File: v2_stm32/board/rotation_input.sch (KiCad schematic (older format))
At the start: 0 parts

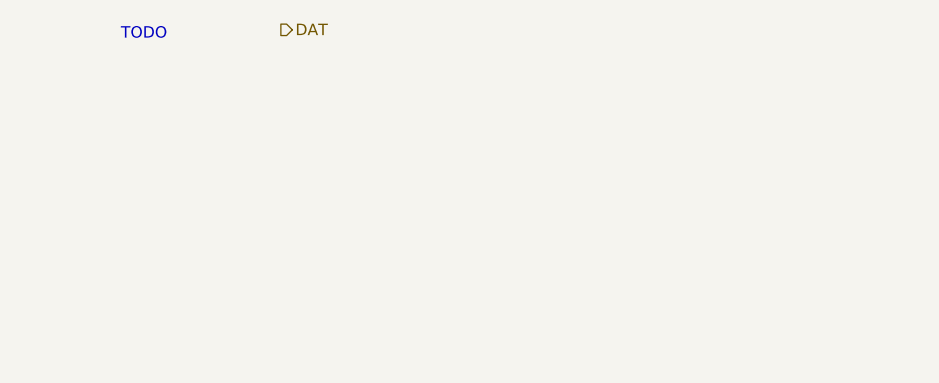
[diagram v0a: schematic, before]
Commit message: Schematic finished (V0.1), Added footprints
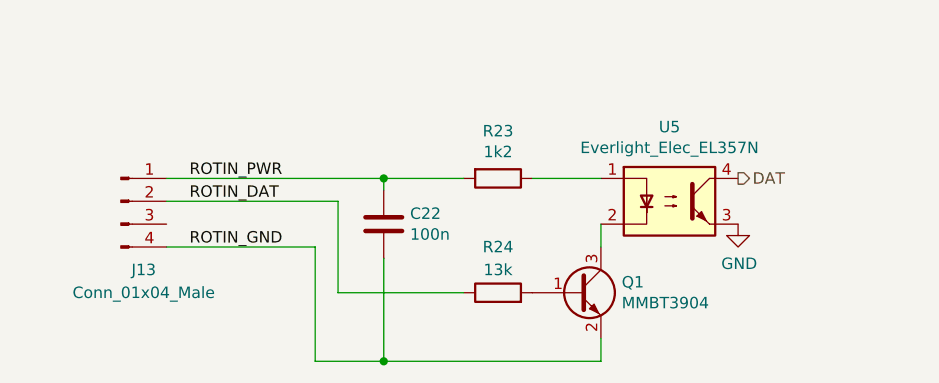
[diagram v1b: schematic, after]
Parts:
- added C22: 100n, Capacitor_SMD:C_0603_1608Metric, symbol Device:C
- added J13: Conn_01x04_Male, Connector_PinHeader_2.54mm:PinHeader_1x04_P2.54mm_Horizontal, symbol Connector:Conn_01x04_Male
- added Q1: MMBT3904, Package_TO_SOT_SMD:SOT-23, symbol Transistor_BJT:MMBT3904
- added R23: 1k2, Resistor_SMD:R_0805_2012Metric, symbol Device:R
- added R24: 13k, Resistor_SMD:R_0603_1608Metric, symbol Device:R
- added U5: Everlight_Elec_EL357N, Lathecontrol_STM32:SOP-4_4.1x4.4x2.54P, symbol Lathecontrol_STM32:Everlight_Elec_EL357N
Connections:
- net DAT: now also U5.4
- new net: Q1.1 (B), R24.2
- new net: Q1.3 (C), U5.2
- new net: R23.1, U5.1
- new net GND: U5.3
- new net ROTIN_DAT: J13.2 (Pin_2), R24.1
- new net ROTIN_GND: C22.2, J13.4 (Pin_4), Q1.2 (E)
- new net ROTIN_PWR: C22.1, J13.1 (Pin_1), R23.2
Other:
- note removed: "TODO"
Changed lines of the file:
@@
 Comment4 ""
 $EndDescr
-Text HLabel 2500 1150 2    50   Output ~ 0
+Text HLabel 4500 1800 2    50   Output ~ 0
 DAT
-Text Notes 1800 1200 0    50   ~ 0
-TODO
+$Comp
+L Lathecontrol_STM32:Everlight_Elec_EL357N U5
+U 1 1 60817786
+P 4200 1900
+F 0 "U5" H 4200 2225 50  0000 C CNN
+F 1 "Everlight_Elec_EL357N" H 4200 2134 50  0000 C CNN
+F 2 "Lathecontrol_STM32:SOP-4_4.1x4.4x2.54P" H 4000 1700 50  0001 L CIN
+F 3 "https://datasheet.lcsc.com/szlcsc/Everlight-Elec-EL357N-B-TA-G_C6649.pdf" H 4200 1900 50  0001 L CNN
+F 4 "C6649" H 4200 1900 50  0001 C CNN "LCSC"
+	1    4200 1900
+	1    0    0    -1
+$EndComp
+$Comp
+L power:GND #PWR089
+U 1 1 6034BC3E
+P 4500 2000
+F 0 "#PWR089" H 4500 1750 50  0001 C CNN
+F 1 "GND" H 4505 1827 50  0000 C CNN
+F 2 "" H 4500 2000 50  0001 C CNN
+F 3 "" H 4500 2000 50  0001 C CNN
+	1    4500 2000
+	1    0    0    -1
+$EndComp
+$Comp
+L Transistor_BJT:MMBT3904 Q1
+U 1 1 60328B9E
+P 3800 2300
+F 0 "Q1" H 3991 2346 50  0000 L CNN
+F 1 "MMBT3904" H 3991 2255 50  0000 L CNN
+F 2 "Package_TO_SOT_SMD:SOT-23" H 4000 2225 50  0001 L CIN
+F 3 "https://www.onsemi.com/pub/Collateral/2N3903-D.PDF" H 3800 2300 50  0001 L CNN
+	1    3800 2300
+	1    0    0    -1
+$EndComp
+Wire Wire Line
+	3900 2000 3900 2100
+$Comp
+L Device:R R23
+U 1 1 6032C873
+P 3450 1800
+F 0 "R23" V 3243 1800 50  0000 C CNN
+F 1 "1k2" V 3334 1800 50  0000 C CNN
+F 2 "Resistor_SMD:R_0805_2012Metric" V 3380 1800 50  0001 C CNN
+F 3 "https://datasheet.lcsc.com/szlcsc/Uniroyal-Elec-0805W8F1201T5E_C17379.pdf" H 3450 1800 50  0001 C CNN
+F 4 "C17379" V 3450 1800 50  0001 C CNN "LCSC"
+	1    3450 1800
+	0    1    1    0
+$EndComp
+Wire Wire Line
+	3600 1800 3900 1800
+$Comp
+L Connector:Conn_01x04_Male J13
+U 1 1 6032E605
+P 1800 1900
+F 0 "J13" H 1900 1600 50  0000 C CNN
+F 1 "Conn_01x04_Male" H 1900 1500 50  0000 C CNN
+F 2 "Connector_PinHeader_2.54mm:PinHeader_1x04_P2.54mm_Horizontal" H 1800 1900 50  0001 C CNN
+F 3 "~" H 1800 1900 50  0001 C CNN
+	1    1800 1900
+	1    0    0    -1
+$EndComp
+Wire Wire Line
+	3900 2500 3900 2600
+Text Label 2100 1800 0    50   ~ 0
+ROTIN_PWR
+Wire Wire Line
+	2750 1900 2750 2300
+Wire Wire Line
+	2000 1900 2750 1900
+Wire Wire Line
+	2000 2100 2650 2100
+Wire Wire Line
+	2650 2100 2650 2600
+Text Label 2100 1900 0    50   ~ 0
+ROTIN_DAT
+Text Label 2100 2100 0    50   ~ 0
+ROTIN_GND
+$Comp
+L Device:C C?
+U 1 1 60340E1E
+P 2950 2000
+AR Path="/6025D9E2/60340E1E" Ref="C?"  Part="1"
+AR Path="/6025D9E2/6025E7C0/60340E1E" Ref="C?"  Part="1"
+AR Path="/6025D9E2/60265A76/60340E1E" Ref="C?"  Part="1"
+AR Path="/6025D9E2/60265B58/60340E1E" Ref="C?"  Part="1"
+AR Path="/6025D9E2/60265BB4/60340E1E" Ref="C?"  Part="1"
+AR Path="/6025D9E2/60265C25/60340E1E" Ref="C?"  Part="1"
+AR Path="/60265C89/60340E1E" Ref="C?"  Part="1"
+AR Path="/60265F6D/60340E1E" Ref="C?"  Part="1"
+AR Path="/60265FC9/60340E1E" Ref="C?"  Part="1"
+AR Path="/6026601C/60340E1E" Ref="C?"  Part="1"
+AR Path="/60340E1E" Ref="C?"  Part="1"
+AR Path="/604E4D29/60340E1E" Ref="C22"  Part="1"
+F 0 "C22" H 3065 2046 50  0000 L CNN
+F 1 "100n" H 3065 1955 50  0000 L CNN
+F 2 "Capacitor_SMD:C_0603_1608Metric" H 2988 1850 50  0001 C CNN
+F 3 "https://datasheet.lcsc.com/szlcsc/YAGEO-CC0603KRX7R9BB104_C14663.pdf" H 2950 2000 50  0001 C CNN
+F 4 "C14663" H 2950 2000 50  0001 C CNN "LCSC"
+	1    2950 2000
+	1    0    0    -1
+$EndComp
+Wire Wire Line
+	2000 1800 2950 1800
+Wire Wire Line
+	2950 1800 2950 1850
+Connection ~ 2950 1800
+Wire Wire Line
+	2950 1800 3300 1800
+Wire Wire Line
+	2950 2150 2950 2600
+Wire Wire Line
+	2950 2600 3900 2600
+Wire Wire Line
+	2650 2600 2950 2600
+Connection ~ 2950 2600
+Wire Wire Line
+	2750 2300 3300 2300
+$Comp
+L Device:R R?
+U 1 1 6037DC52
+P 3450 2300
+AR Path="/6025D9E2/6037DC52" Ref="R?"  Part="1"
+AR Path="/6025D9E2/6025E7C0/6037DC52" Ref="R?"  Part="1"
+AR Path="/6025D9E2/60265A76/6037DC52" Ref="R?"  Part="1"
+AR Path="/6025D9E2/60265B58/6037DC52" Ref="R?"  Part="1"
+AR Path="/6025D9E2/60265BB4/6037DC52" Ref="R?"  Part="1"
+AR Path="/6025D9E2/60265C25/6037DC52" Ref="R?"  Part="1"
+AR Path="/60265C89/6037DC52" Ref="R?"  Part="1"
+AR Path="/60265F6D/6037DC52" Ref="R?"  Part="1"
+AR Path="/60265FC9/6037DC52" Ref="R?"  Part="1"
+AR Path="/6026601C/6037DC52" Ref="R?"  Part="1"
+AR Path="/604E4D29/6037DC52" Ref="R24"  Part="1"
+F 0 "R24" V 3650 2300 50  0000 C CNN
+F 1 "13k" V 3550 2300 50  0000 C CNN
+F 2 "Resistor_SMD:R_0603_1608Metric" V 3380 2300 50  0001 C CNN
+F 3 "~" H 3450 2300 50  0001 C CNN
+F 4 "C22797" H 3450 2300 50  0001 C CNN "LCSC"
+	1    3450 2300
+	0    -1   -1   0
+$EndComp
 $EndSCHEMATC

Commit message: More routing
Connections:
- net ROTIN_DAT: now also J13.3 (Pin_3); no longer J13.2 (Pin_2)
- net ROTIN_GND: now also J13.1 (Pin_1); no longer J13.4 (Pin_4)
- net ROTIN_PWR: now also J13.4 (Pin_4); no longer J13.1 (Pin_1)
- no-connect marks 0 -> 1
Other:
- moved on the sheet: C22, J13, Q1, R23, R24, U5
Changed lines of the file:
@@
 Comment4 ""
 $EndDescr
-Text HLabel 4500 1800 2    50   Output ~ 0
+Text HLabel 3600 1450 2    50   Output ~ 0
 DAT
 $Comp
 L Lathecontrol_STM32:Everlight_Elec_EL357N U5
 U 1 1 60817786
-P 4200 1900
-F 0 "U5" H 4200 2225 50  0000 C CNN
-F 1 "Everlight_Elec_EL357N" H 4200 2134 50  0000 C CNN
-F 2 "Lathecontrol_STM32:SOP-4_4.1x4.4x2.54P" H 4000 1700 50  0001 L CIN
-F 3 "https://datasheet.lcsc.com/szlcsc/Everlight-Elec-EL357N-B-TA-G_C6649.pdf" H 4200 1900 50  0001 L CNN
-F 4 "C6649" H 4200 1900 50  0001 C CNN "LCSC"
-	1    4200 1900
+P 3300 1550
+F 0 "U5" H 3300 1875 50  0000 C CNN
+F 1 "Everlight_Elec_EL357N" H 3300 1784 50  0000 C CNN
+F 2 "Lathecontrol_STM32:SOP-4_4.1x4.4x2.54P" H 3100 1350 50  0001 L CIN
+F 3 "https://datasheet.lcsc.com/szlcsc/Everlight-Elec-EL357N-B-TA-G_C6649.pdf" H 3300 1550 50  0001 L CNN
+F 4 "C6649" H 3300 1550 50  0001 C CNN "LCSC"
+	1    3300 1550
 	1    0    0    -1
 $EndComp
@@
 L power:GND #PWR089
 U 1 1 6034BC3E
-P 4500 2000
-F 0 "#PWR089" H 4500 1750 50  0001 C CNN
-F 1 "GND" H 4505 1827 50  0000 C CNN
-F 2 "" H 4500 2000 50  0001 C CNN
-F 3 "" H 4500 2000 50  0001 C CNN
-	1    4500 2000
+P 3600 1650
+F 0 "#PWR089" H 3600 1400 50  0001 C CNN
+F 1 "GND" H 3605 1477 50  0000 C CNN
+F 2 "" H 3600 1650 50  0001 C CNN
+F 3 "" H 3600 1650 50  0001 C CNN
+	1    3600 1650
 	1    0    0    -1
 $EndComp
@@
 L Transistor_BJT:MMBT3904 Q1
 U 1 1 60328B9E
-P 3800 2300
-F 0 "Q1" H 3991 2346 50  0000 L CNN
-F 1 "MMBT3904" H 3991 2255 50  0000 L CNN
-F 2 "Package_TO_SOT_SMD:SOT-23" H 4000 2225 50  0001 L CIN
-F 3 "https://www.onsemi.com/pub/Collateral/2N3903-D.PDF" H 3800 2300 50  0001 L CNN
-	1    3800 2300
+P 2900 1950
+F 0 "Q1" H 3091 1996 50  0000 L CNN
+F 1 "MMBT3904" H 3091 1905 50  0000 L CNN
+F 2 "Package_TO_SOT_SMD:SOT-23" H 3100 1875 50  0001 L CIN
+F 3 "https://www.onsemi.com/pub/Collateral/2N3903-D.PDF" H 2900 1950 50  0001 L CNN
+	1    2900 1950
 	1    0    0    -1
 $EndComp
 Wire Wire Line
-	3900 2000 3900 2100
+	3000 1650 3000 1750
 $Comp
 L Device:R R23
 U 1 1 6032C873
-P 3450 1800
-F 0 "R23" V 3243 1800 50  0000 C CNN
-F 1 "1k2" V 3334 1800 50  0000 C CNN
-F 2 "Resistor_SMD:R_0805_2012Metric" V 3380 1800 50  0001 C CNN
-F 3 "https://datasheet.lcsc.com/szlcsc/Uniroyal-Elec-0805W8F1201T5E_C17379.pdf" H 3450 1800 50  0001 C CNN
-F 4 "C17379" V 3450 1800 50  0001 C CNN "LCSC"
-	1    3450 1800
+P 2550 1450
+F 0 "R23" V 2343 1450 50  0000 C CNN
+F 1 "1k2" V 2434 1450 50  0000 C CNN
+F 2 "Resistor_SMD:R_0805_2012Metric" V 2480 1450 50  0001 C CNN
+F 3 "https://datasheet.lcsc.com/szlcsc/Uniroyal-Elec-0805W8F1201T5E_C17379.pdf" H 2550 1450 50  0001 C CNN
+F 4 "C17379" V 2550 1450 50  0001 C CNN "LCSC"
+	1    2550 1450
 	0    1    1    0
 $EndComp
 Wire Wire Line
-	3600 1800 3900 1800
+	2700 1450 3000 1450
 $Comp
 L Connector:Conn_01x04_Male J13
 U 1 1 6032E605
-P 1800 1900
-F 0 "J13" H 1900 1600 50  0000 C CNN
-F 1 "Conn_01x04_Male" H 1900 1500 50  0000 C CNN
-F 2 "Connector_PinHeader_2.54mm:PinHeader_1x04_P2.54mm_Horizontal" H 1800 1900 50  0001 C CNN
-F 3 "~" H 1800 1900 50  0001 C CNN
-	1    1800 1900
+P 4600 1750
+F 0 "J13" H 4700 1450 50  0000 C CNN
+F 1 "Conn_01x04_Male" H 4700 1350 50  0000 C CNN
+F 2 "Connector_PinHeader_2.54mm:PinHeader_1x04_P2.54mm_Horizontal" H 4600 1750 50  0001 C CNN
+F 3 "~" H 4600 1750 50  0001 C CNN
+	1    4600 1750
 	1    0    0    -1
 $EndComp
 Wire Wire Line
-	3900 2500 3900 2600
-Text Label 2100 1800 0    50   ~ 0
-ROTIN_PWR
-Wire Wire Line
-	2750 1900 2750 2300
-Wire Wire Line
-	2000 1900 2750 1900
-Wire Wire Line
-	2000 2100 2650 2100
-Wire Wire Line
-	2650 2100 2650 2600
-Text Label 2100 1900 0    50   ~ 0
+	3000 2150 3000 2250
+Text Label 1850 1950 2    50   ~ 0
 ROTIN_DAT
-Text Label 2100 2100 0    50   ~ 0
+Text Label 1850 2250 2    50   ~ 0
 ROTIN_GND
 $Comp
 L Device:C C?
 U 1 1 60340E1E
-P 2950 2000
+P 2050 1650
 AR Path="/6025D9E2/60340E1E" Ref="C?"  Part="1"
 AR Path="/6025D9E2/6025E7C0/60340E1E" Ref="C?"  Part="1"
@@
 AR Path="/60340E1E" Ref="C?"  Part="1"
 AR Path="/604E4D29/60340E1E" Ref="C22"  Part="1"
-F 0 "C22" H 3065 2046 50  0000 L CNN
-F 1 "100n" H 3065 1955 50  0000 L CNN
-F 2 "Capacitor_SMD:C_0603_1608Metric" H 2988 1850 50  0001 C CNN
-F 3 "https://datasheet.lcsc.com/szlcsc/YAGEO-CC0603KRX7R9BB104_C14663.pdf" H 2950 2000 50  0001 C CNN
-F 4 "C14663" H 2950 2000 50  0001 C CNN "LCSC"
-	1    2950 2000
+F 0 "C22" H 2165 1696 50  0000 L CNN
+F 1 "100n" H 2165 1605 50  0000 L CNN
+F 2 "Capacitor_SMD:C_0603_1608Metric" H 2088 1500 50  0001 C CNN
+F 3 "https://datasheet.lcsc.com/szlcsc/YAGEO-CC0603KRX7R9BB104_C14663.pdf" H 2050 1650 50  0001 C CNN
+F 4 "C14663" H 2050 1650 50  0001 C CNN "LCSC"
+	1    2050 1650
 	1    0    0    -1
 $EndComp
 Wire Wire Line
-	2000 1800 2950 1800
+	1850 1450 2050 1450
 Wire Wire Line
-	2950 1800 2950 1850
-Connection ~ 2950 1800
+	2050 1450 2050 1500
+Connection ~ 2050 1450
 Wire Wire Line
-	2950 1800 3300 1800
+	2050 1450 2400 1450
 Wire Wire Line
-	2950 2150 2950 2600
+	2050 1800 2050 2250
 Wire Wire Line
-	2950 2600 3900 2600
+	2050 2250 3000 2250
 Wire Wire Line
-	2650 2600 2950 2600
-Connection ~ 2950 2600
-Wire Wire Line
-	2750 2300 3300 2300
+	1850 1950 2400 1950
 $Comp
 L Device:R R?
 U 1 1 6037DC52
-P 3450 2300
+P 2550 1950
 AR Path="/6025D9E2/6037DC52" Ref="R?"  Part="1"
 AR Path="/6025D9E2/6025E7C0/6037DC52" Ref="R?"  Part="1"
@@
 AR Path="/6026601C/6037DC52" Ref="R?"  Part="1"
 AR Path="/604E4D29/6037DC52" Ref="R24"  Part="1"
-F 0 "R24" V 3650 2300 50  0000 C CNN
-F 1 "13k" V 3550 2300 50  0000 C CNN
-F 2 "Resistor_SMD:R_0603_1608Metric" V 3380 2300 50  0001 C CNN
-F 3 "~" H 3450 2300 50  0001 C CNN
-F 4 "C22797" H 3450 2300 50  0001 C CNN "LCSC"
-	1    3450 2300
+F 0 "R24" V 2750 1950 50  0000 C CNN
+F 1 "13k" V 2650 1950 50  0000 C CNN
+F 2 "Resistor_SMD:R_0603_1608Metric" V 2480 1950 50  0001 C CNN
+F 3 "~" H 2550 1950 50  0001 C CNN
+F 4 "C22797" H 2550 1950 50  0001 C CNN "LCSC"
+	1    2550 1950
 	0    -1   -1   0
 $EndComp
+Wire Wire Line
+	1850 2250 2050 2250
+Connection ~ 2050 2250
+Text Label 4800 1650 0    50   ~ 0
+ROTIN_GND
+Text Label 1850 1450 2    50   ~ 0
+ROTIN_PWR
+Text Label 4800 1950 0    50   ~ 0
+ROTIN_PWR
+Text Label 4800 1850 0    50   ~ 0
+ROTIN_DAT
+NoConn ~ 4800 1750
 $EndSCHEMATC
